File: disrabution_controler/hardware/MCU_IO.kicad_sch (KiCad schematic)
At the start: 60 parts, among them J1 Conn_Coaxial, Q1 NMOS, U1 TJA1043T/1J, U2 ESP32-S2FH2, U3 PI4IOE5V6416LEX, U4 ECMF02-2AMX6, Y1 40 MHz

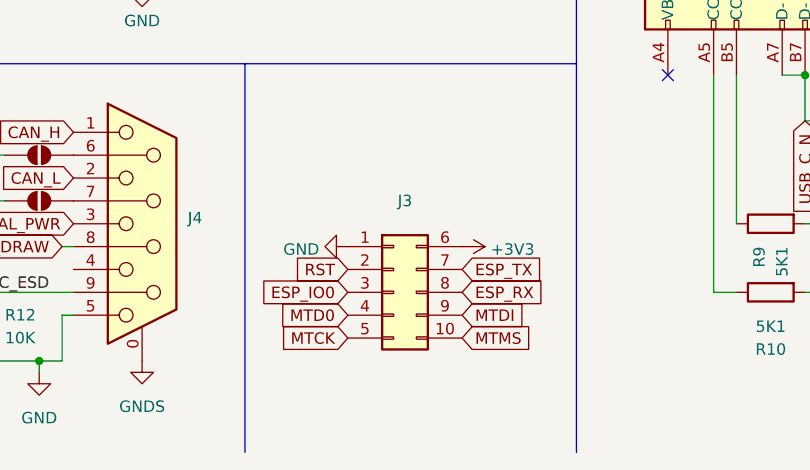
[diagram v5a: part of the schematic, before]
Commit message: fixed programing connector
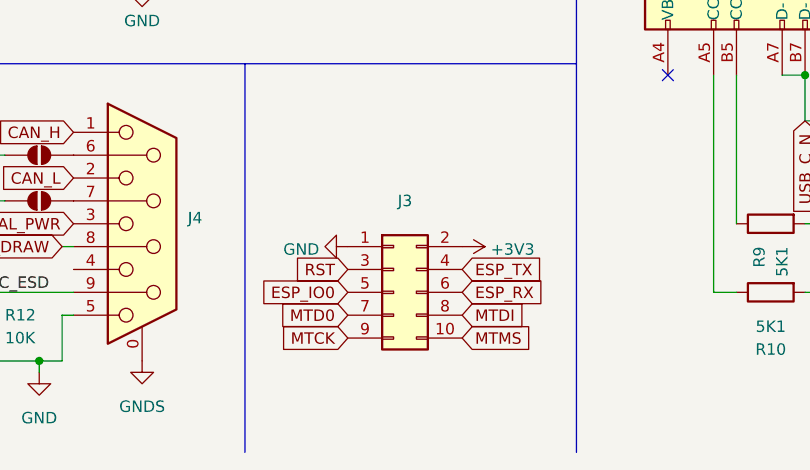
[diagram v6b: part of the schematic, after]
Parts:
- removed J3: ~, Connector_PinHeader_2.54mm:PinHeader_2x05_P2.54mm_Vertical, symbol Connector_Generic:Conn_02x05_Top_Bottom
- added J3: ~, Connector_PinHeader_2.54mm:PinHeader_2x05_P2.54mm_Vertical, symbol Connector_Generic:Conn_02x05_Odd_Even
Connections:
- net +3V3: now also J3.2 (Pin_2)
- net ESP_IO0: now also J3.5 (Pin_5)
- net ESP_RX: now also J3.6 (Pin_6)
- net ESP_TX: now also J3.4 (Pin_4)
- net GND: now also J3.1 (Pin_1)
- net MTCK: now also J3.9 (Pin_9)
- net MTD0: now also J3.7 (Pin_7)
- net MTDI: now also J3.8 (Pin_8)
- net MTMS: now also J3.10 (Pin_10)
- net RST: now also J3.3 (Pin_3)
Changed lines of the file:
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@@
 	)
 	(symbol
+		(lib_id "Connector_Generic:Conn_02x05_Odd_Even")
+		(at 90.17 180.34 0)
+		(unit 1)
+		(exclude_from_sim no)
+		(in_bom yes)
+		(on_board yes)
+		(dnp no)
+		(fields_autoplaced yes)
+		(property "Reference" "J3"
+			(at 91.44 170.18 0)
+			(effects
+				(font
+					(size 1.27 1.27)
+				)
+			)
+		)
+		(property "Value" "~"
+			(at 91.44 172.72 0)
+			(effects
+				(font
+					(size 1.27 1.27)
+				)
+			)
+		)
+		(property "Footprint" "Connector_PinHeader_2.54mm:PinHeader_2x05_P2.54mm_Vertical"
+			(at 90.17 180.34 0)
+			(effects
+				(font
+					(size 1.27 1.27)
+				)
+				(hide yes)
+			)
+		)
+		(property "Datasheet" "~"
+			(at 90.17 180.34 0)
+			(effects
+				(font
+					(size 1.27 1.27)
+				)
+				(hide yes)
+			)
+		)
+		(property "Description" "Generic connector, double row, 02x05, odd/even pin numbering scheme (row 1 odd numbers, row 2 even numbers), script generated (kicad-library-utils/schlib/autogen/connector/)"
+			(at 90.17 180.34 0)
+			(effects
+				(font
+					(size 1.27 1.27)
+				)
+				(hide yes)
+			)
+		)
+		(property "Digikey Part Number" "S9169-ND"
+			(at 90.17 180.34 0)
+			(effects
+				(font
+					(size 1.27 1.27)
+				)
+				(hide yes)
+			)
+		)
+		(pin "6"
+		)
+		(pin "8"
+		)
+		(pin "4"
+		)
+		(pin "9"
+		)
+		(pin "2"
+		)
+		(pin "10"
+		)
+		(pin "7"
+		)
+		(pin "5"
+		)
+		(pin "3"
+		)
+		(pin "1"
+		)
+		(instances
+			(project "distrabution_controler"
+				(path "/2800815a-f06a-4e36-93dc-fea3151edeb4/cc9feaf5-e3f6-4501-9fb5-0cfb07e51032"
+					(reference "J3")
+					(unit 1)
+				)
+			)
+		)
+	)
+	(symbol
 		(lib_id "power:GND")
 		(at 85.09 175.26 270)
@@
 					(unit 1)
 				)
-			)
-		)
-	)
-	(symbol
-		(lib_id "Connector_Generic:Conn_02x05_Top_Bottom")
-		(at 90.17 180.34 0)
-		(unit 1)
-		(exclude_from_sim no)
-		(in_bom yes)
-		(on_board yes)
-		(dnp no)
-		(fields_autoplaced yes)
-		(property "Reference" "J3"
-			(at 91.44 170.18 0)
-			(effects
-				(font
-					(size 1.27 1.27)
-				)
-			)
-		)
-		(property "Value" "~"
-			(at 91.44 172.72 0)
-			(effects
-				(font
-					(size 1.27 1.27)
-				)
-			)
-		)
-		(property "Footprint" "Connector_PinHeader_2.54mm:PinHeader_2x05_P2.54mm_Vertical"
-			(at 90.17 180.34 0)
-			(effects
-				(font
-					(size 1.27 1.27)
-				)
-				(hide yes)
-			)
-		)
-		(property "Datasheet" "~"
-			(at 90.17 180.34 0)
-			(effects
-				(font
-					(size 1.27 1.27)
-				)
-				(hide yes)
-			)
-		)
-		(property "Description" "Generic connector, double row, 02x05, top/bottom pin numbering scheme (row 1: 1...pins_per_row, row2: pins_per_row+1 ... num_pins), script generated (kicad-library-utils/schlib/autogen/connector/)"
-			(at 90.17 180.34 0)
-			(effects
-				(font
-					(size 1.27 1.27)
-				)
-				(hide yes)
-			)
-		)
-		(pin "9"
-		)
-		(pin "8"
-		)
-		(pin "2"
-		)
-		(pin "6"
-		)
-		(pin "5"
-		)
-		(pin "3"
-		)
-		(pin "4"
-		)
-		(pin "7"
-		)
-		(pin "10"
-		)
-		(pin "1"
-		)
-		(instances
-			(project "distrabution_controler"
-				(path "/2800815a-f06a-4e36-93dc-fea3151edeb4/cc9feaf5-e3f6-4501-9fb5-0cfb07e51032"
-					(reference "J3")
-					(unit 1)
-				)
